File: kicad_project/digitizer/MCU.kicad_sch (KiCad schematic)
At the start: 18 parts, among them J401 Conn_02x05_Odd_Even, U401 ATSAM4E8EA-AN

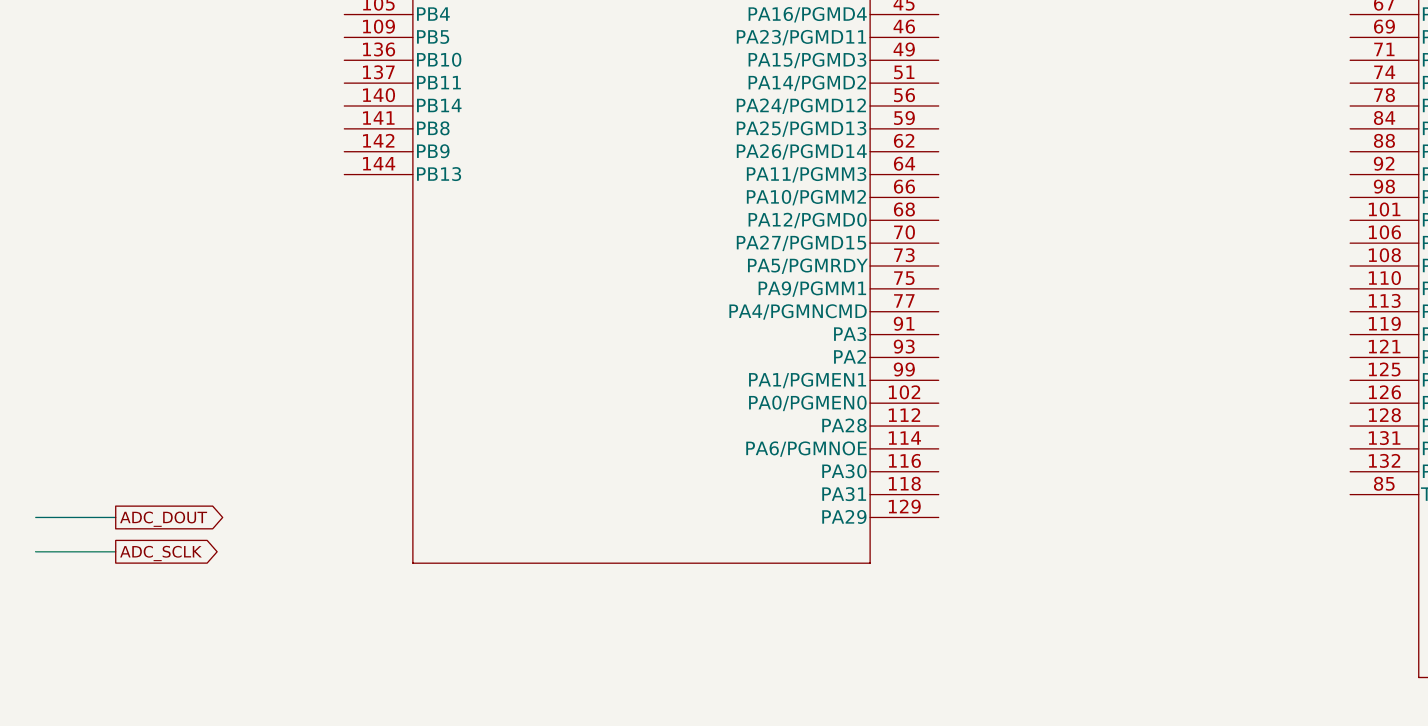
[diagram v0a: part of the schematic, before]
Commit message: connected the ADC I2C lines
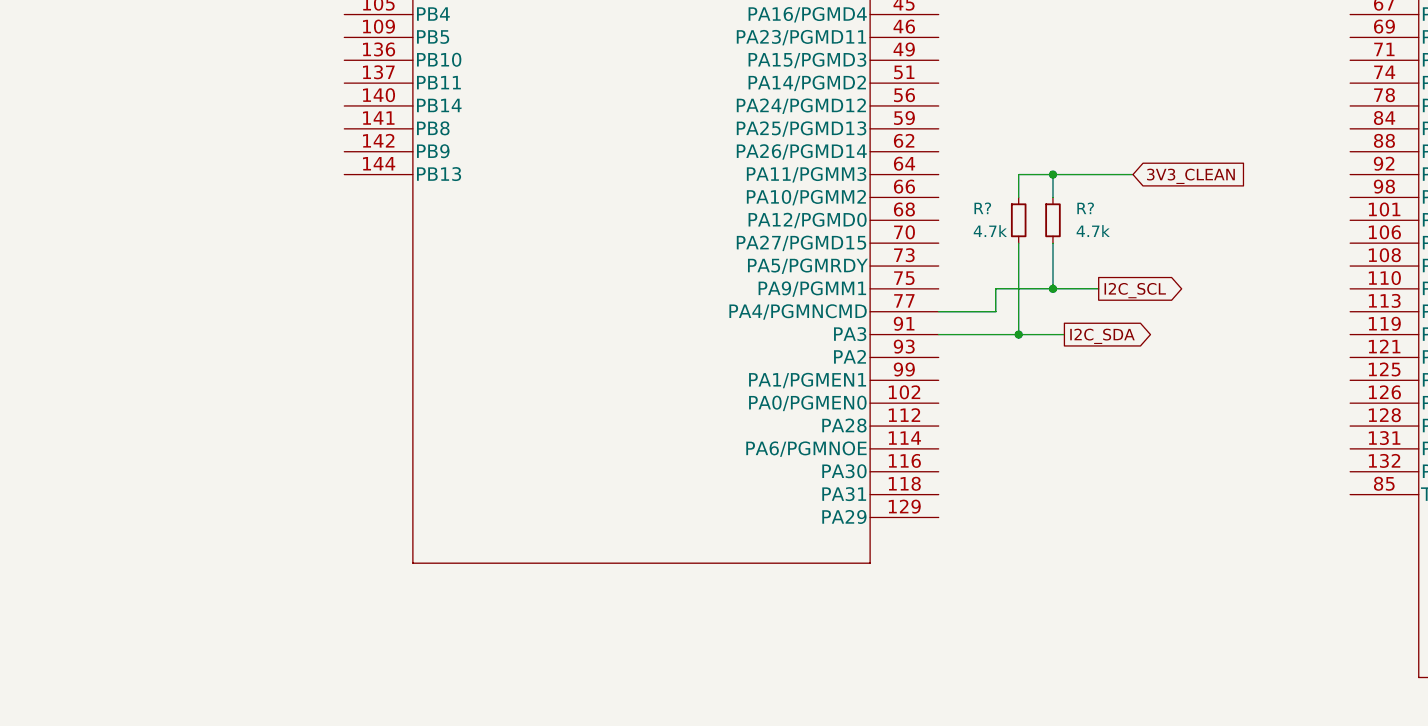
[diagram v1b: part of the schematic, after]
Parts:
- added R? (x2): 4.7k, Resistor_SMD:R_2512_6332Metric_Pad1.40x3.35mm_HandSolder, symbol Device:R_Small
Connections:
- net 3V3_CLEAN: now also R?.1, R?.1
- net I2C_SCL: now reaches U401.77 (PA4/PGMNCMD)
- net I2C_SCL: now also R?.2
- net I2C_SDA: now reaches U401.91 (PA3)
- net I2C_SDA: now also R?.2
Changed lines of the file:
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@@
   (junction (at 228.6 30.48) (diameter 0) (color 0 0 0 0)
   )
+  (junction (at 134.62 86.36) (diameter 0) (color 0 0 0 0)
+  )
   (junction (at 261.62 151.13) (diameter 0) (color 0 0 0 0)
   )
   (junction (at 241.3 35.56) (diameter 0) (color 0 0 0 0)
   )
+  (junction (at 130.81 91.44) (diameter 0) (color 0 0 0 0)
+  )
   (junction (at 241.3 83.82) (diameter 0) (color 0 0 0 0)
   )
@@
   (junction (at 220.98 151.13) (diameter 0) (color 0 0 0 0)
   )
+  (junction (at 134.62 73.66) (diameter 0) (color 0 0 0 0)
+  )
   (junction (at 241.3 91.44) (diameter 0) (color 0 0 0 0)
   )
@@
   (junction (at 241.3 50.8) (diameter 0) (color 0 0 0 0)
   )
-  (wire (pts (xy 21.59 115.57) (xy 30.48 115.57))
-    (stroke (width 0) (type default) (color 0 0 0 0))
-  )
   (wire (pts (xy 198.12 151.13) (xy 198.12 148.59))
     (stroke (width 0) (type default) (color 0 0 0 0))
@@
     (stroke (width 0) (type default) (color 0 0 0 0))
   )
+  (wire (pts (xy 121.92 91.44) (xy 130.81 91.44))
+    (stroke (width 0) (type default) (color 0 0 0 0))
+  )
   (wire (pts (xy 205.74 148.59) (xy 205.74 151.13))
     (stroke (width 0) (type default) (color 0 0 0 0))
@@
     (stroke (width 0) (type default) (color 0 0 0 0))
   )
+  (wire (pts (xy 128.27 86.36) (xy 134.62 86.36))
+    (stroke (width 0) (type default) (color 0 0 0 0))
+  )
   (wire (pts (xy 241.3 63.5) (xy 241.3 66.04))
     (stroke (width 0) (type default) (color 0 0 0 0))
@@
     (stroke (width 0) (type default) (color 0 0 0 0))
   )
+  (wire (pts (xy 130.81 81.28) (xy 130.81 91.44))
+    (stroke (width 0) (type default) (color 0 0 0 0))
+  )
   (wire (pts (xy 254 140.97) (xy 261.62 140.97))
     (stroke (width 0) (type default) (color 0 0 0 0))
@@
     (stroke (width 0) (type default) (color 0 0 0 0))
   )
+  (wire (pts (xy 134.62 73.66) (xy 143.51 73.66))
+    (stroke (width 0) (type default) (color 0 0 0 0))
+  )
   (wire (pts (xy 205.74 140.97) (xy 213.36 140.97))
     (stroke (width 0) (type default) (color 0 0 0 0))
@@
     (stroke (width 0) (type default) (color 0 0 0 0))
   )
+  (wire (pts (xy 134.62 86.36) (xy 139.7 86.36))
+    (stroke (width 0) (type default) (color 0 0 0 0))
+  )
   (wire (pts (xy 261.62 151.13) (xy 254 151.13))
     (stroke (width 0) (type default) (color 0 0 0 0))
@@
     (stroke (width 0) (type default) (color 0 0 0 0))
   )
+  (wire (pts (xy 130.81 91.44) (xy 135.89 91.44))
+    (stroke (width 0) (type default) (color 0 0 0 0))
+  )
+  (wire (pts (xy 130.81 73.66) (xy 134.62 73.66))
+    (stroke (width 0) (type default) (color 0 0 0 0))
+  )
   (wire (pts (xy 269.24 151.13) (xy 261.62 151.13))
     (stroke (width 0) (type default) (color 0 0 0 0))
@@
     (stroke (width 0) (type default) (color 0 0 0 0))
   )
+  (wire (pts (xy 134.62 73.66) (xy 134.62 76.2))
+    (stroke (width 0) (type default) (color 0 0 0 0))
+  )
   (wire (pts (xy 241.3 96.52) (xy 241.3 105.41))
     (stroke (width 0) (type default) (color 0 0 0 0))
@@
     (stroke (width 0) (type default) (color 0 0 0 0))
   )
+  (wire (pts (xy 134.62 81.28) (xy 134.62 86.36))
+    (stroke (width 0) (type default) (color 0 0 0 0))
+  )
   (wire (pts (xy 234.95 71.12) (xy 234.95 76.2))
     (stroke (width 0) (type default) (color 0 0 0 0))
@@
     (stroke (width 0) (type default) (color 0 0 0 0))
   )
+  (wire (pts (xy 128.27 88.9) (xy 128.27 86.36))
+    (stroke (width 0) (type default) (color 0 0 0 0))
+  )
   (wire (pts (xy 213.36 140.97) (xy 213.36 143.51))
     (stroke (width 0) (type default) (color 0 0 0 0))
@@
     (stroke (width 0) (type default) (color 0 0 0 0))
   )
-  (wire (pts (xy 21.59 111.76) (xy 30.48 111.76))
+  (wire (pts (xy 121.92 88.9) (xy 128.27 88.9))
     (stroke (width 0) (type default) (color 0 0 0 0))
   )
   (wire (pts (xy 234.95 71.12) (xy 241.3 71.12))
+    (stroke (width 0) (type default) (color 0 0 0 0))
+  )
+  (wire (pts (xy 130.81 76.2) (xy 130.81 73.66))
     (stroke (width 0) (type default) (color 0 0 0 0))
   )
@@
     )
   )
-  (global_label "ADC_SCLK" (shape output) (at 30.48 115.57 0) (fields_autoplaced)
+  (global_label "I2C_SCL" (shape output) (at 139.7 86.36 0) (fields_autoplaced)
     (effects (font (size 1.27 1.27)) (justify left))
-    (property "Intersheet References" "${INTERSHEET_REFS}" (id 0) (at 42.2669 115.4906 0)
+    (property "Intersheet References" "${INTERSHEET_REFS}" (id 0) (at 149.6726 86.2806 0)
       (effects (font (size 1.27 1.27)) (justify left) hide)
     )
@@
     )
   )
-  (global_label "ADC_DOUT" (shape output) (at 30.48 111.76 0) (fields_autoplaced)
+  (global_label "I2C_SDA" (shape output) (at 135.89 91.44 0) (fields_autoplaced)
     (effects (font (size 1.27 1.27)) (justify left))
-    (property "Intersheet References" "${INTERSHEET_REFS}" (id 0) (at 42.3879 111.6806 0)
+    (property "Intersheet References" "${INTERSHEET_REFS}" (id 0) (at 145.9231 91.3606 0)
       (effects (font (size 1.27 1.27)) (justify left) hide)
     )
@@
     (effects (font (size 1.27 1.27)) (justify left))
     (property "Intersheet References" "${INTERSHEET_REFS}" (id 0) (at 221.3974 43.1006 0)
+      (effects (font (size 1.27 1.27)) (justify left) hide)
+    )
+  )
+  (global_label "3V3_CLEAN" (shape input) (at 143.51 73.66 0) (fields_autoplaced)
+    (effects (font (size 1.27 1.27)) (justify left))
+    (property "Intersheet References" "${INTERSHEET_REFS}" (id 0) (at 156.2645 73.7394 0)
       (effects (font (size 1.27 1.27)) (justify left) hide)
     )
@@
     )
     (property "Datasheet" "~" (id 3) (at 234.95 52.07 0)
+      (effects (font (size 1.27 1.27)) hide)
+    )
+    (pin "1")
+    (pin "2")
+  )
+  (symbol (lib_id "Device:R_Small") (at 134.62 78.74 0) (unit 1)
+    (in_bom yes) (on_board yes) (fields_autoplaced)
+    (property "Reference" "R?" (id 0) (at 137.16 77.4699 0)
+      (effects (font (size 1.27 1.27)) (justify left))
+    )
+    (property "Value" "4.7k" (id 1) (at 137.16 80.0099 0)
+      (effects (font (size 1.27 1.27)) (justify left))
+    )
+    (property "Footprint" "Resistor_SMD:R_2512_6332Metric_Pad1.40x3.35mm_HandSolder" (id 2) (at 134.62 78.74 0)
+      (effects (font (size 1.27 1.27)) hide)
+    )
+    (property "Datasheet" "~" (id 3) (at 134.62 78.74 0)
       (effects (font (size 1.27 1.27)) hide)
     )
@@
       (effects (font (size 1.27 1.27)) hide)
     )
+    (pin "1")
+    (pin "2")
+  )
+  (symbol (lib_id "Device:R_Small") (at 130.81 78.74 0) (unit 1)
+    (in_bom yes) (on_board yes)
+    (property "Reference" "R?" (id 0) (at 125.73 77.47 0)
+      (effects (font (size 1.27 1.27)) (justify left))
+    )
+    (property "Value" "4.7k" (id 1) (at 125.73 80.01 0)
+      (effects (font (size 1.27 1.27)) (justify left))
+    )
+    (property "Footprint" "Resistor_SMD:R_2512_6332Metric_Pad1.40x3.35mm_HandSolder" (id 2) (at 130.81 78.74 0)
+      (effects (font (size 1.27 1.27)) hide)
+    )
+    (property "Datasheet" "~" (id 3) (at 130.81 78.74 0)
+      (effects (font (size 1.27 1.27)) hide)
+    )

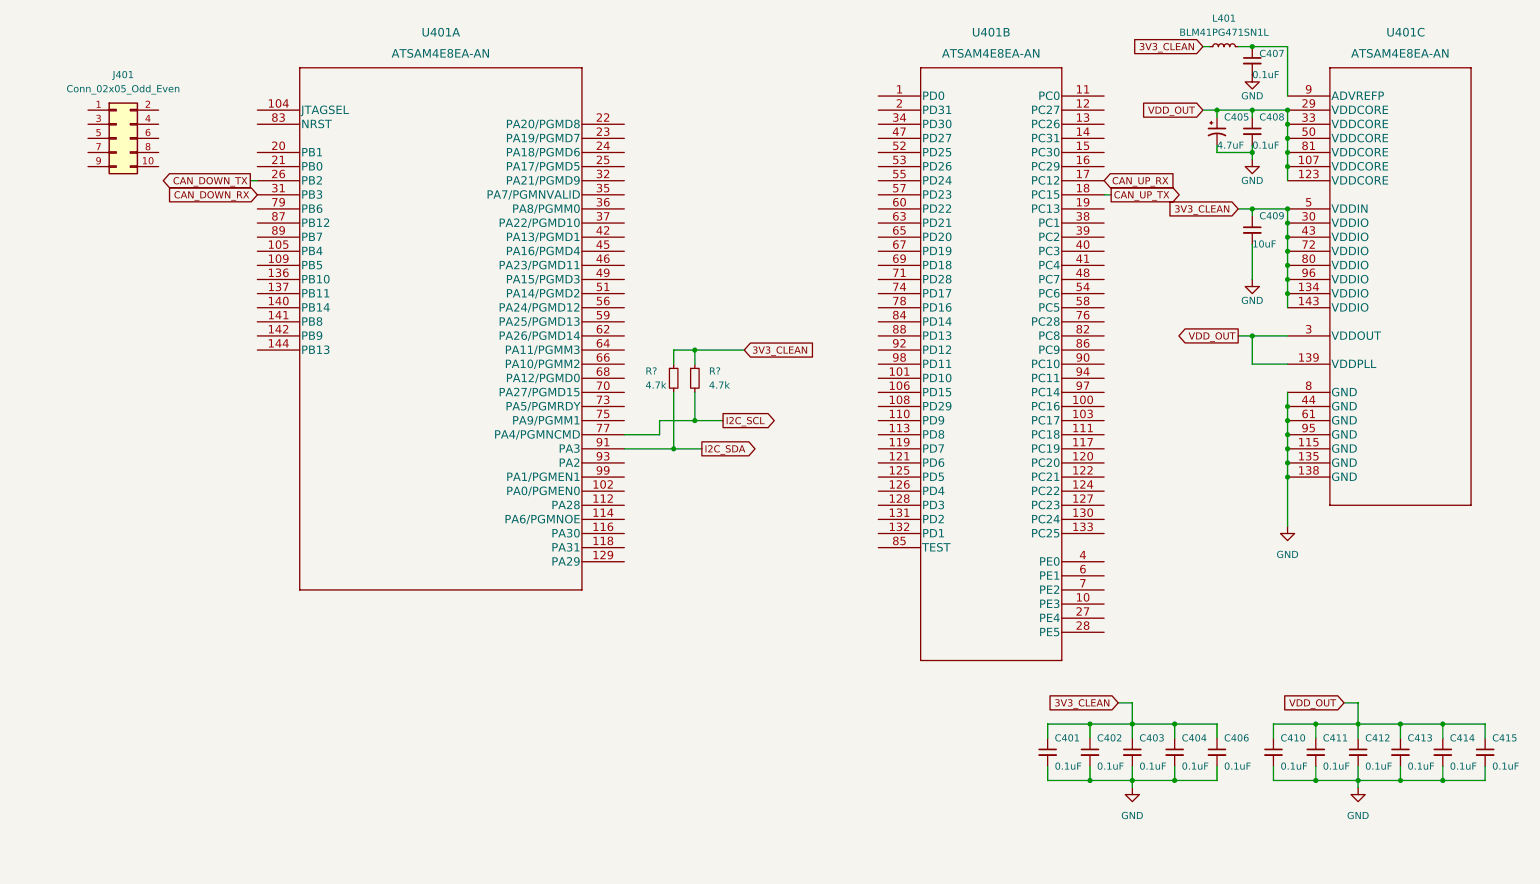
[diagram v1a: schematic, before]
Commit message: added the JTAG and Reset circuitry
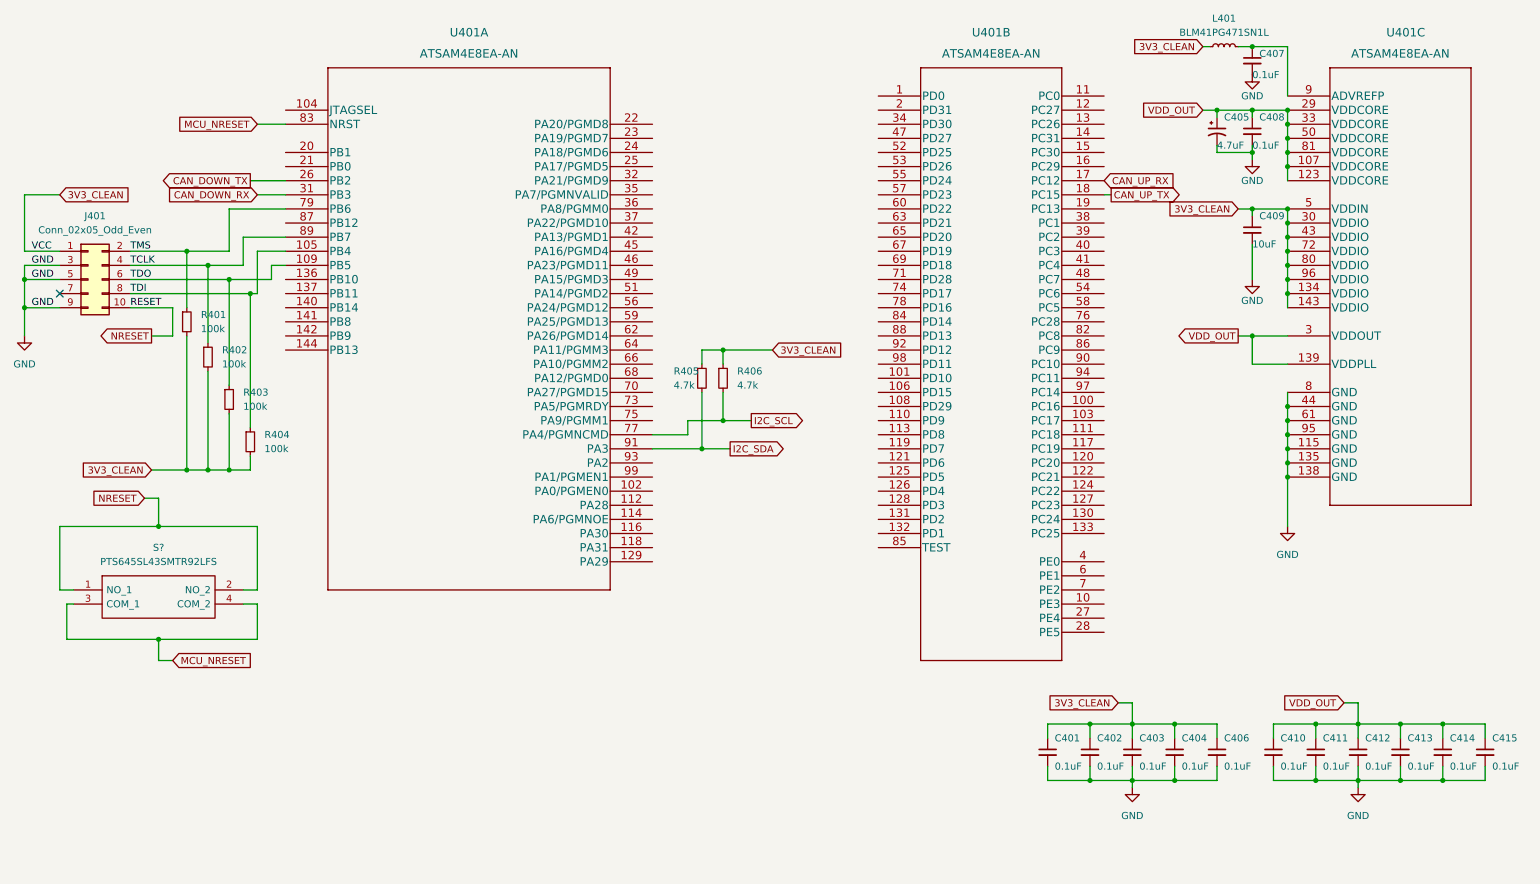
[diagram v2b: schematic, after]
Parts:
- added R401, R402, R403, R404: 100k, Resistor_SMD:R_2512_6332Metric_Pad1.40x3.35mm_HandSolder, symbol Device:R_Small
- added S?: PTS645SL43SMTR92LFS, PTS645SL43SMTR92LFS, symbol SamacSys_Parts:PTS645SL43SMTR92LFS
- gave numbers to parts that had none: 2
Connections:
- net 3V3_CLEAN: now also J401.1 (Pin_1), R401.2, R402.2, R403.2, R404.2
- net GND: now also J401.3 (Pin_3), J401.5 (Pin_5), J401.9 (Pin_9)
- net NRESET: now reaches J401.10 (Pin_10)
- net NRESET: now also S?.1 (NO_1), S?.2 (NO_2)
- net TMS: now reaches J401.2 (Pin_2)
- net TMS: now also U401.79 (PB6), R401.1
- net TCLK: now reaches J401.4 (Pin_4)
- net TCLK: now also U401.89 (PB7), R402.1
- net TDO: now reaches J401.6 (Pin_6)
- net TDO: now also U401.109 (PB5), R403.1
- net TDI: now reaches J401.8 (Pin_8)
- net TDI: now also U401.105 (PB4), R404.1
- net MCU_NRESET: now reaches U401.83 (NRST)
- net MCU_NRESET: now also S?.3 (COM_1), S?.4 (COM_2)
- no-connect marks 0 -> 1
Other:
- moved on the sheet: J401, R405, R406, U401A

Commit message: fixed the reset switch circuitry, added labels to CAN lines
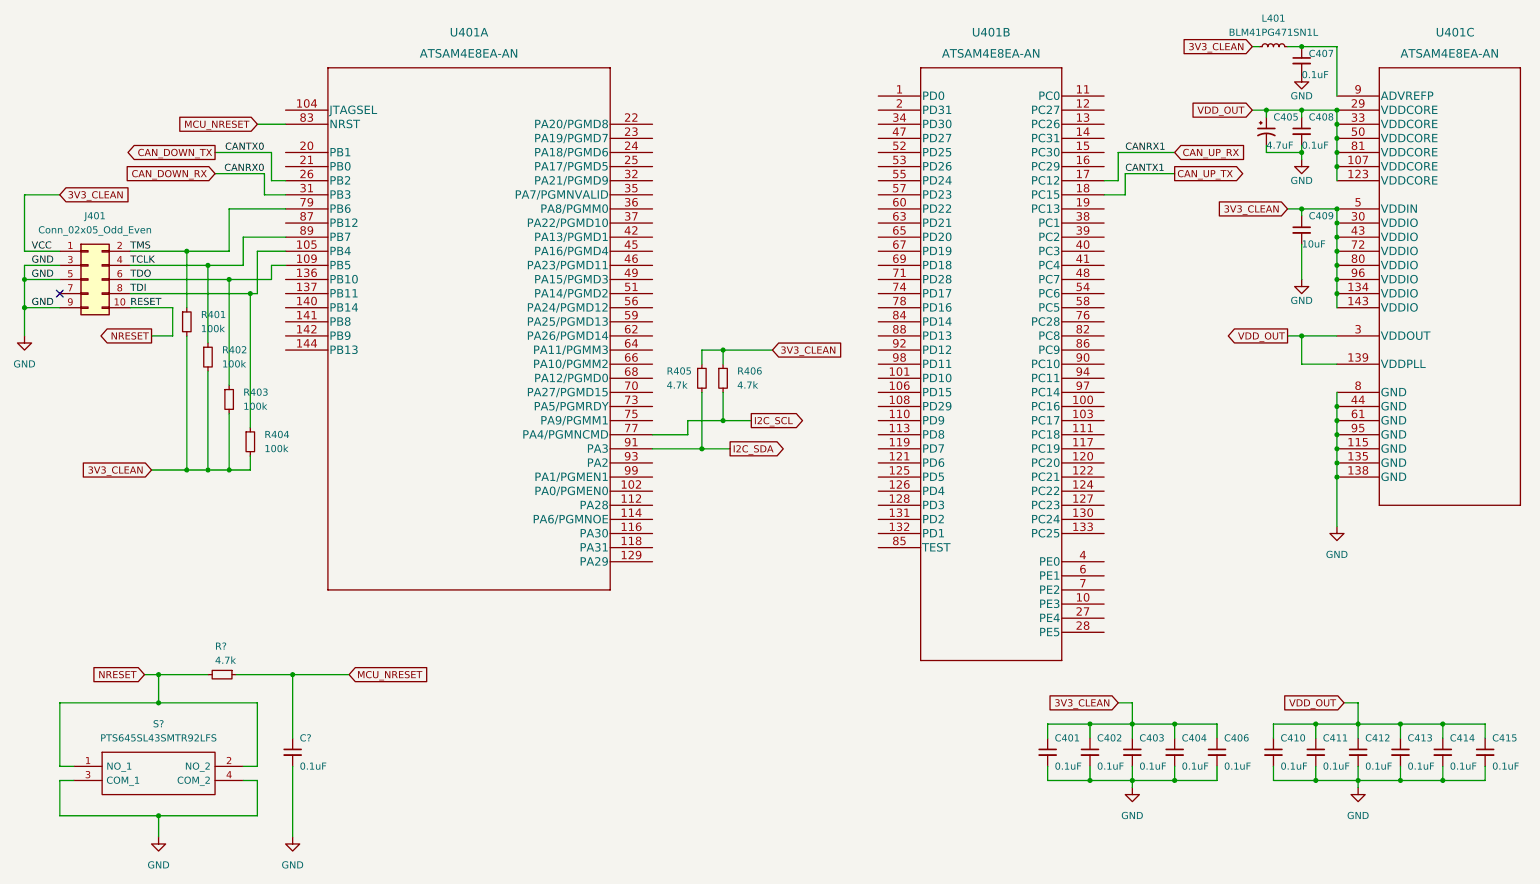
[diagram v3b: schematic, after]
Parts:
- added C?: 0.1uF, Capacitor_SMD:C_2220_5650Metric_Pad1.97x5.40mm_HandSolder, symbol Device:C_Small
- added R?: 4.7k, Resistor_SMD:R_2512_6332Metric_Pad1.40x3.35mm_HandSolder, symbol Device:R_Small
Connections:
- net GND: now also S?.3 (COM_1), S?.4 (COM_2), C?.2
- net MCU_NRESET: now also C?.1, R?.1; no longer S?.3 (COM_1), S?.4 (COM_2)
- net NRESET: now also R?.2
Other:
- moved on the sheet: C405, C407, C408, C409, L401, S?, U401C
